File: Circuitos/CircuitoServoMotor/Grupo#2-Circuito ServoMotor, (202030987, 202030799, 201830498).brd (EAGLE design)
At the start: 150.1 x 76.2 mm, 8 parts, among them U1 ARDUINO-UNO-R3-SHIELD

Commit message: Modificamos archivo del servo
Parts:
- moved R1 8.39 mm to (121.5, 8.97), turned to 270 degrees
- moved R3 8.39 mm to (103.7, 8.97), turned to 90 degrees
- moved R2 8.39 mm to (139.3, 8.97), turned to 270 degrees
- moved SERVO2 0.95 mm to (111.4, 70.2)
- moved U1 0.95 mm to (47.9, 30.8)
- moved S1 0.95 mm to (106.2, 28.0)
- moved S2 0.95 mm to (124.0, 28.0)
- moved S3 0.95 mm to (141.8, 28.0)
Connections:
- net U1_5V: now also R1.2, R2.2; no longer R1.1, R2.1
- net U1_D4: now also R1.1; no longer R1.2
- net U1_D5: now also R2.1; no longer R2.2
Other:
- board size 150.1 x 76.2 mm -> 150.1 x 77.1 mm
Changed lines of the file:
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@@
 <plain>
 <wire x1="0" y1="0" x2="150.05156820633442" y2="0" width="0" layer="20"/>
-<wire x1="150.05156820633442" y1="0" x2="150.05156820633442" y2="76.1939379188484" width="0" layer="20"/>
-<wire x1="150.05156820633442" y1="76.1939379188484" x2="0" y2="76.1939379188484" width="0" layer="20"/>
-<wire x1="0" y1="76.1939379188484" x2="0" y2="0" width="0" layer="20"/>
+<wire x1="150.05156820633442" y1="0" x2="150.05156820633442" y2="77.13976675752048" width="0" layer="20"/>
+<wire x1="150.05156820633442" y1="77.13976675752048" x2="0" y2="77.13976675752048" width="0" layer="20"/>
+<wire x1="0" y1="77.13976675752048" x2="0" y2="0" width="0" layer="20"/>
 </plain>
 <attributes/>
@@
 </autorouter>
 <elements>
-<element name="S3" library="Tinkercad" package="SWITCH-MOMENTARY-PTH-6.5MM" package3d_urn="urn:adsk.eagle:package:32246662/2" value="SWITCH_MOMENTARY" x="141.7966" y="27.0742" rot="R90" smashed="yes"/>
-<element name="S2" library="Tinkercad" package="SWITCH-MOMENTARY-PTH-6.5MM" package3d_urn="urn:adsk.eagle:package:32246662/2" value="SWITCH_MOMENTARY" x="124.0166" y="27.0742" rot="R90" smashed="yes"/>
-<element name="R1" library="Tinkercad" package="RESAD1016W63L850D250B" package3d_urn="urn:adsk.eagle:package:31513020/1" value="10k" x="116.3966" y="15.6442" rot="R360" smashed="yes"/>
-<element name="R2" library="Tinkercad" package="RESAD1016W63L850D250B" package3d_urn="urn:adsk.eagle:package:31513020/1" value="10k" x="134.1766" y="15.6442" rot="R360" smashed="yes"/>
-<element name="SERVO2" library="Tinkercad" package="SG90" package3d_urn="urn:adsk.eagle:package:32659983/1" value="SERVOSG90" x="111.3563" y="69.2089" rot="R180" smashed="yes"/>
-<element name="U1" library="Tinkercad" package="ARDUINO-UNO-R3-SHIELD" package3d_urn="urn:adsk.eagle:package:32092383/3" value="ARDUINO-UNO-R3-SHIELD" x="47.885" y="29.845" rot="R270" smashed="yes"/>
-<element name="R3" library="Tinkercad" package="RESAD1016W63L850D250B" package3d_urn="urn:adsk.eagle:package:31513020/1" value="10k" x="98.6166" y="15.6442" rot="R360" smashed="yes"/>
-<element name="S1" library="Tinkercad" package="SWITCH-MOMENTARY-PTH-6.5MM" package3d_urn="urn:adsk.eagle:package:32246662/2" value="SWITCH_MOMENTARY" x="106.2366" y="27.0742" rot="R90" smashed="yes"/>
+<element name="S3" library="Tinkercad" package="SWITCH-MOMENTARY-PTH-6.5MM" package3d_urn="urn:adsk.eagle:package:32246662/2" value="SWITCH_MOMENTARY" x="141.7966" y="28.02" rot="R90" smashed="yes"/>
+<element name="S2" library="Tinkercad" package="SWITCH-MOMENTARY-PTH-6.5MM" package3d_urn="urn:adsk.eagle:package:32246662/2" value="SWITCH_MOMENTARY" x="124.0166" y="28.02" rot="R90" smashed="yes"/>
+<element name="R1" library="Tinkercad" package="RESAD1016W63L850D250B" package3d_urn="urn:adsk.eagle:package:31513020/1" value="10k" x="121.4766" y="8.97" rot="R270" smashed="yes"/>
+<element name="R2" library="Tinkercad" package="RESAD1016W63L850D250B" package3d_urn="urn:adsk.eagle:package:31513020/1" value="10k" x="139.2566" y="8.97" rot="R270" smashed="yes"/>
+<element name="SERVO2" library="Tinkercad" package="SG90" package3d_urn="urn:adsk.eagle:package:32659983/1" value="SERVOSG90" x="111.3563" y="70.1548" rot="R180" smashed="yes"/>
+<element name="U1" library="Tinkercad" package="ARDUINO-UNO-R3-SHIELD" package3d_urn="urn:adsk.eagle:package:32092383/3" value="ARDUINO-UNO-R3-SHIELD" x="47.885" y="30.7908" rot="R270" smashed="yes"/>
+<element name="R3" library="Tinkercad" package="RESAD1016W63L850D250B" package3d_urn="urn:adsk.eagle:package:31513020/1" value="10k" x="103.6966" y="8.97" rot="R90" smashed="yes"/>
+<element name="S1" library="Tinkercad" package="SWITCH-MOMENTARY-PTH-6.5MM" package3d_urn="urn:adsk.eagle:package:32246662/2" value="SWITCH_MOMENTARY" x="106.2366" y="28.02" rot="R90" smashed="yes"/>
 </elements>
 <signals>
@@
 <contactref element="U1" pad="GND@1"/>
 <contactref element="U1" pad="GND@2"/>
+<contactref element="S1" pad="3"/>
 <contactref element="S3" pad="3"/>
-<contactref element="S1" pad="3"/>
-<wire x1="50.425" y1="5.715" x2="52.965" y2="5.715" width="0" layer="19" extent="1-1"/>
-<wire x1="50.425" y1="5.715" x2="36.455" y2="53.975" width="0" layer="19" extent="1-1"/>
-<wire x1="52.965" y1="5.715" x2="108.4972" y2="23.823" width="0" layer="19" extent="1-1"/>
-<wire x1="108.4972" y1="30.3254" x2="108.4972" y2="23.823" width="0" layer="19" extent="1-1"/>
-<wire x1="108.4972" y1="30.3254" x2="126.2772" y2="30.3254" width="0" layer="19" extent="1-1"/>
-<wire x1="126.2772" y1="30.3254" x2="126.2772" y2="23.823" width="0" layer="19" extent="1-1"/>
-<wire x1="126.2772" y1="30.3254" x2="144.0572" y2="30.3254" width="0" layer="19" extent="1-1"/>
-<wire x1="144.0572" y1="30.3254" x2="144.0572" y2="23.823" width="0" layer="19" extent="1-1"/>
-<wire x1="108.4972" y1="30.3254" x2="113.8963" y2="69.2089" width="0" layer="19" extent="1-1"/>
+<wire x1="50.425" y1="6.6608" x2="52.965" y2="6.6608" width="0" layer="19" extent="1-1"/>
+<wire x1="50.425" y1="6.6608" x2="36.455" y2="54.9208" width="0" layer="19" extent="1-1"/>
+<wire x1="52.965" y1="6.6608" x2="108.4972" y2="24.7688" width="0" layer="19" extent="1-1"/>
+<wire x1="108.4972" y1="31.2712" x2="108.4972" y2="24.7688" width="0" layer="19" extent="1-1"/>
+<wire x1="108.4972" y1="31.2712" x2="126.2772" y2="31.2712" width="0" layer="19" extent="1-1"/>
+<wire x1="126.2772" y1="31.2712" x2="126.2772" y2="24.7688" width="0" layer="19" extent="1-1"/>
+<wire x1="126.2772" y1="31.2712" x2="144.0572" y2="31.2712" width="0" layer="19" extent="1-1"/>
+<wire x1="144.0572" y1="31.2712" x2="144.0572" y2="24.7688" width="0" layer="19" extent="1-1"/>
+<wire x1="108.4972" y1="31.2712" x2="113.8963" y2="70.1548" width="0" layer="19" extent="1-1"/>
 </signal>
 <signal name="U1_D5">
-<contactref element="R2" pad="2"/>
 <contactref element="S3" pad="1"/>
+<contactref element="R2" pad="1"/>
 <contactref element="S3" pad="2"/>
 <contactref element="U1" pad="D5"/>
-<wire x1="139.536" y1="23.823" x2="139.536" y2="30.3254" width="0" layer="19" extent="1-1"/>
-<wire x1="139.2566" y1="15.6442" x2="139.536" y2="23.823" width="0" layer="19" extent="1-1"/>
-<wire x1="139.536" y1="30.3254" x2="60.585" y2="53.975" width="0" layer="19" extent="1-1"/>
+<wire x1="139.536" y1="24.7688" x2="139.536" y2="31.2712" width="0" layer="19" extent="1-1"/>
+<wire x1="139.536" y1="24.7688" x2="139.2566" y2="14.05" width="0" layer="19" extent="1-1"/>
+<wire x1="139.536" y1="31.2712" x2="60.585" y2="54.9208" width="0" layer="19" extent="1-1"/>
 </signal>
 <signal name="U1_D4">
@@
 <contactref element="U1" pad="D4"/>
 <contactref element="S2" pad="1"/>
+<contactref element="R1" pad="1"/>
+<wire x1="121.756" y1="31.2712" x2="121.756" y2="24.7688" width="0" layer="19" extent="1-1"/>
+<wire x1="121.756" y1="24.7688" x2="121.4766" y2="14.05" width="0" layer="19" extent="1-1"/>
+<wire x1="121.756" y1="31.2712" x2="63.125" y2="54.9208" width="0" layer="19" extent="1-1"/>
+</signal>
+<signal name="U1_5V">
+<contactref element="U1" pad="5V"/>
+<contactref element="R3" pad="1"/>
 <contactref element="R1" pad="2"/>
-<wire x1="121.756" y1="30.3254" x2="121.756" y2="23.823" width="0" layer="19" extent="1-1"/>
-<wire x1="121.756" y1="23.823" x2="121.4766" y2="15.6442" width="0" layer="19" extent="1-1"/>
-<wire x1="121.756" y1="30.3254" x2="63.125" y2="53.975" width="0" layer="19" extent="1-1"/>
-</signal>
-<signal name="U1_5V">
-<contactref element="R2" pad="1"/>
-<contactref element="U1" pad="5V"/>
 <contactref element="SERVO2" pad="2"/>
-<contactref element="R1" pad="1"/>
-<contactref element="R3" pad="1"/>
-<wire x1="111.3166" y1="15.6442" x2="93.5366" y2="15.6442" width="0" layer="19" extent="1-1"/>
-<wire x1="129.0966" y1="15.6442" x2="111.3166" y2="15.6442" width="0" layer="19" extent="1-1"/>
-<wire x1="47.885" y1="5.715" x2="93.5366" y2="15.6442" width="0" layer="19" extent="1-1"/>
-<wire x1="111.3563" y1="69.2089" x2="111.3166" y2="15.6442" width="0" layer="19" extent="1-1"/>
+<contactref element="R2" pad="2"/>
+<wire x1="121.4766" y1="3.89" x2="139.2566" y2="3.89" width="0" layer="19" extent="1-1"/>
+<wire x1="103.6966" y1="3.89" x2="121.4766" y2="3.89" width="0" layer="19" extent="1-1"/>
+<wire x1="47.885" y1="6.6608" x2="103.6966" y2="3.89" width="0" layer="19" extent="1-1"/>
+<wire x1="103.6966" y1="3.89" x2="111.3563" y2="70.1548" width="0" layer="19" extent="1-1"/>
 </signal>
 <signal name="U1_D2">
 <contactref element="SERVO2" pad="3"/>
 <contactref element="U1" pad="D2"/>
-<wire x1="108.8163" y1="69.2089" x2="68.205" y2="53.975" width="0" layer="19" extent="1-1"/>
+<wire x1="108.8163" y1="70.1548" x2="68.205" y2="54.9208" width="0" layer="19" extent="1-1"/>
 </signal>
 <signal name="U1_D3">
@@
 <contactref element="S1" pad="1"/>
 <contactref element="R3" pad="2"/>
-<wire x1="103.976" y1="30.3254" x2="103.976" y2="23.823" width="0" layer="19" extent="1-1"/>
-<wire x1="103.976" y1="23.823" x2="103.6966" y2="15.6442" width="0" layer="19" extent="1-1"/>
-<wire x1="103.976" y1="30.3254" x2="65.665" y2="53.975" width="0" layer="19" extent="1-1"/>
+<wire x1="103.976" y1="31.2712" x2="103.976" y2="24.7688" width="0" layer="19" extent="1-1"/>
+<wire x1="103.976" y1="24.7688" x2="103.6966" y2="14.05" width="0" layer="19" extent="1-1"/>
+<wire x1="103.976" y1="31.2712" x2="65.665" y2="54.9208" width="0" layer="19" extent="1-1"/>
 </signal>
 </signals>

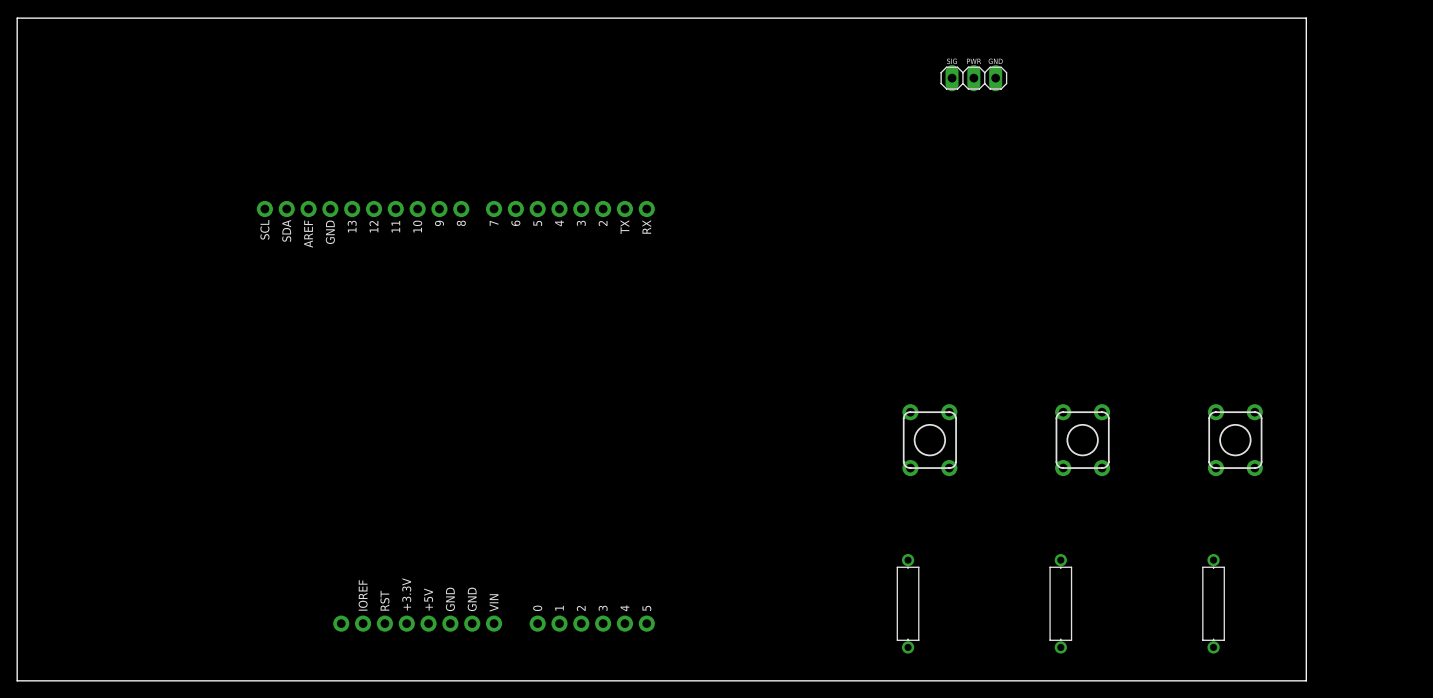
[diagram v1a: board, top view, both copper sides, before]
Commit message: Modificamos el circuito en tinkercad agregando el boton cero grados
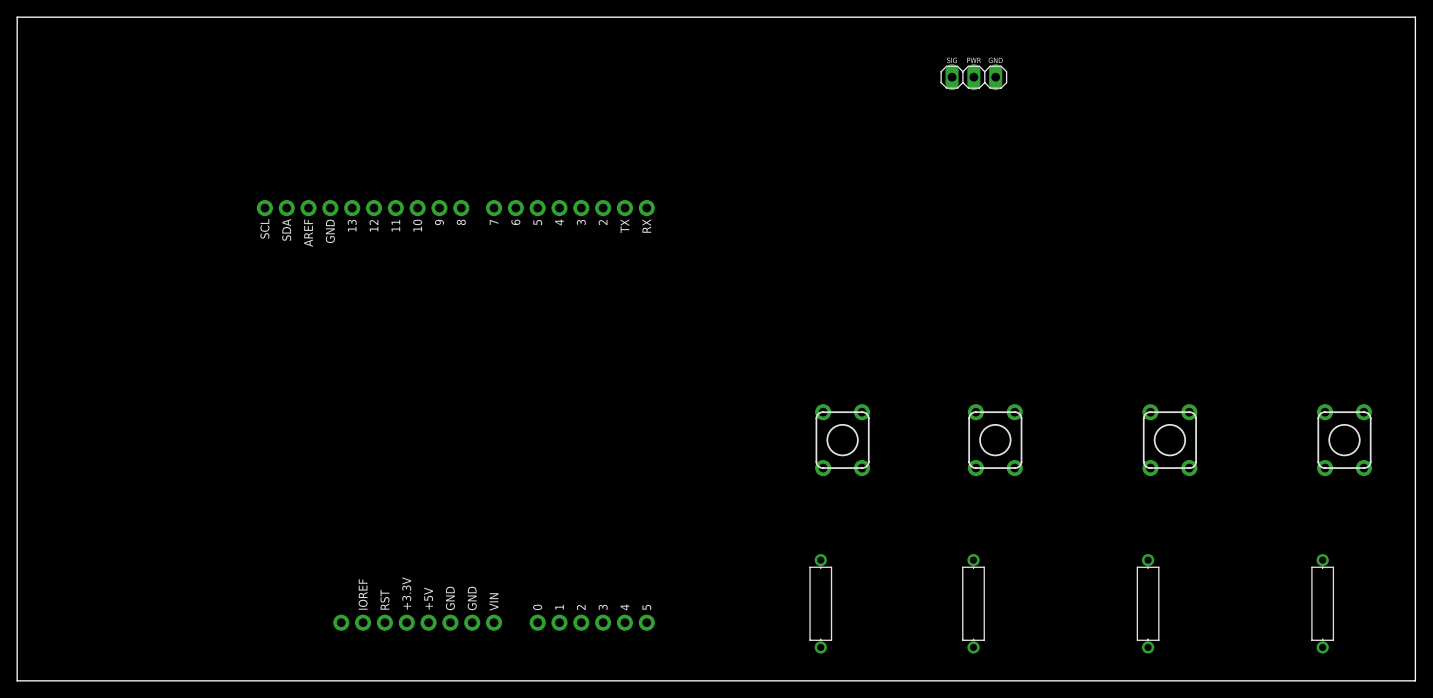
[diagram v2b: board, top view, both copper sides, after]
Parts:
- added R4: 10k, Tinkercad:RESAD1016W63L850D250B
- added S4: SWITCH_MOMENTARY, Tinkercad:SWITCH-MOMENTARY-PTH-6.5MM
- moved R1 10.2 mm to (111.3, 8.97)
- moved R3 10.2 mm to (93.5, 8.97)
- moved S1 10.2 mm to (96.1, 28.0)
- moved S2 10.2 mm to (113.9, 28.0)
- moved R2 7.62 mm to (131.6, 8.97)
- moved S3 7.62 mm to (134.2, 28.0)
- moved SERVO2 0.11 mm to (111.4, 70.3)
- moved U1 0.11 mm to (47.9, 30.9)
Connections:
- new net U1_D6: R3.2, S1.1, S1.2, U1.D6
- net U1_5V: now also R4.2
- net U1_D3: now also R1.1, S2.1, S2.2; no longer R3.2, S1.1, S1.2
- net U1_D4: now also R2.1, S3.1, S3.2; no longer R1.1, S2.1, S2.2
- net U1_D5: now also R4.1, S4.1, S4.2; no longer R2.1, S3.1, S3.2
- net U1_GND: now also S4.3, S4.4
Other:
- board size 150.1 x 77.1 mm -> 162.8 x 77.2 mm
